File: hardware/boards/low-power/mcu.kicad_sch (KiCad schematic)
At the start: 29 parts, among them J6 Conn_01x03_Pin, SW1 SW_Push, U4 RP2040, U5 W25Q128JVPIQ, Y2 12 MHz

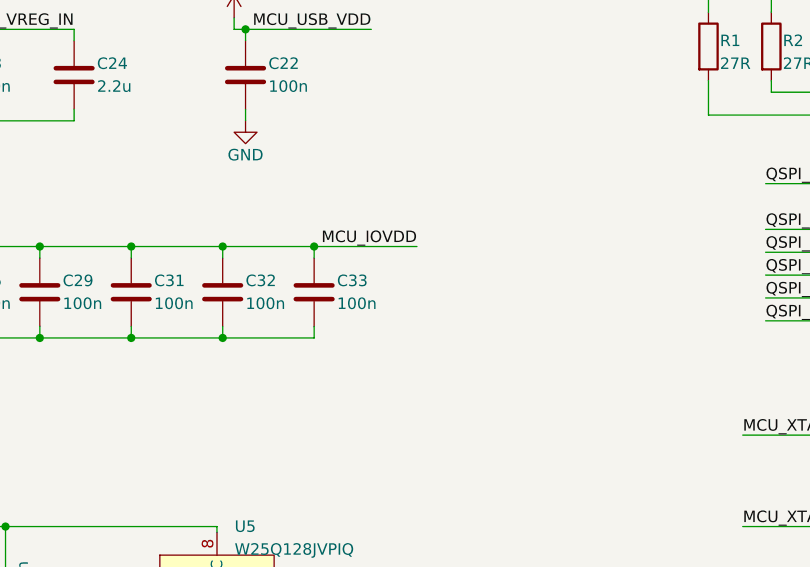
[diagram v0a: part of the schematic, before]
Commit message: Add footprints and models for LP board
Also completed rough layout for LP board to estimate board space usage.
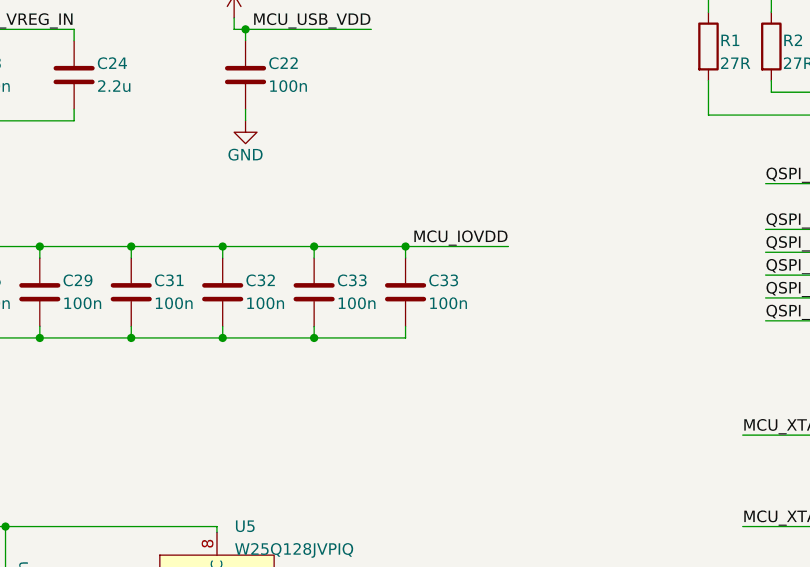
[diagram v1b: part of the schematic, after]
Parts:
- added C33: 100n, Capacitor_SMD:C_0201_0603Metric, symbol Device:C
- C1: footprint Capacitor_SMD:C_0201_0603Metric -> Capacitor_SMD:C_0402_1005Metric
- J6: footprint Connector_PinSocket_1.27mm:PinSocket_1x05_P1.27mm_Vertical -> Connector_PinHeader_1.27mm:PinHeader_1x03_P1.27mm_Vertical
- SW1: footprint (none) -> capstone:R-668048
- U5: footprint capstone:SON127P610X510X80-8N430X340 -> Package_SON:WSON-8-1EP_6x5mm_P1.27mm_EP3.4x4.3mm
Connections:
- net +3V3: now also C33.1
- net GND: now also C33.2
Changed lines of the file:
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@@
   (junction (at 33.655 93.345) (diameter 0) (color 0 0 0 0)
   )
+  (junction (at 74.295 93.345) (diameter 0) (color 0 0 0 0)
+  )
   (junction (at 132.08 134.62) (diameter 0) (color 0 0 0 0)
   )
@@
   (junction (at 59.055 164.465) (diameter 0) (color 0 0 0 0)
   )
+  (junction (at 84.455 83.185) (diameter 0) (color 0 0 0 0)
+  )
   (junction (at 33.655 43.815) (diameter 0) (color 0 0 0 0)
   )
@@
     (stroke (width 0) (type default))
   )
+  (wire (pts (xy 84.455 83.185) (xy 84.455 84.455))
+    (stroke (width 0) (type default))
+  )
   (wire (pts (xy 43.815 33.655) (xy 33.655 33.655))
     (stroke (width 0) (type default))
@@
     (stroke (width 0) (type default))
   )
+  (wire (pts (xy 84.455 92.075) (xy 84.455 93.345))
+    (stroke (width 0) (type default))
+  )
   (wire (pts (xy 66.675 67.945) (xy 66.675 69.215))
     (stroke (width 0) (type default))
@@
     (stroke (width 0) (type default))
   )
-  (wire (pts (xy 74.295 83.185) (xy 85.725 83.185))
+  (wire (pts (xy 74.295 83.185) (xy 84.455 83.185))
     (stroke (width 0) (type default))
   )
@@
     (stroke (width 0) (type default))
   )
+  (wire (pts (xy 84.455 83.185) (xy 95.885 83.185))
+    (stroke (width 0) (type default))
+  )
   (wire (pts (xy 121.92 104.14) (xy 134.62 104.14))
     (stroke (width 0) (type default))
@@
   )
   (wire (pts (xy 264.795 111.125) (xy 264.795 109.855))
+    (stroke (width 0) (type default))
+  )
+  (wire (pts (xy 84.455 93.345) (xy 74.295 93.345))
     (stroke (width 0) (type default))
   )
@@
     (effects (font (size 1.27 1.27)) (justify left bottom))
   )
-  (label "MCU_IOVDD" (at 85.725 83.185 180) (fields_autoplaced)
+  (label "MCU_IOVDD" (at 95.885 83.185 180) (fields_autoplaced)
     (effects (font (size 1.27 1.27)) (justify right bottom))
   )
@@
       (effects (font (size 1.27 1.27)))
     )
-    (property "Footprint" "" (at 45.72 159.385 0)
+    (property "Footprint" "capstone:R-668048" (at 45.72 159.385 0)
       (effects (font (size 1.27 1.27)) hide)
     )
@@
       (effects (font (size 1.27 1.27)) (justify left))
     )
-    (property "Footprint" "capstone:SON127P610X510X80-8N430X340" (at 67.31 127.635 0)
+    (property "Footprint" "Package_SON:WSON-8-1EP_6x5mm_P1.27mm_EP3.4x4.3mm" (at 67.31 127.635 0)
       (effects (font (size 1.27 1.27)) hide)
     )
@@
       (effects (font (size 1.27 1.27)))
     )
-    (property "Footprint" "Connector_PinSocket_1.27mm:PinSocket_1x05_P1.27mm_Vertical" (at 125.095 127 0)
+    (property "Footprint" "Connector_PinHeader_1.27mm:PinHeader_1x03_P1.27mm_Vertical" (at 125.095 127 0)
       (effects (font (size 1.27 1.27)) hide)
     )
@@
       (effects (font (size 1.27 1.27)) (justify left))
     )
-    (property "Footprint" "Capacitor_SMD:C_0201_0603Metric" (at 33.9852 128.27 0)
+    (property "Footprint" "Capacitor_SMD:C_0402_1005Metric" (at 33.9852 128.27 0)
       (effects (font (size 1.27 1.27)) hide)
     )
@@
         )
       )
+    )
+  )
+  (symbol (lib_id "Device:C") (at 84.455 88.265 0) (unit 1)
+    (in_bom yes) (on_board yes) (dnp no)
+    (property "Reference" "C33" (at 86.995 86.995 0)
+      (effects (font (size 1.27 1.27)) (justify left))
+    )
+    (property "Value" "100n" (at 86.995 89.535 0)
+      (effects (font (size 1.27 1.27)) (justify left))
+    )
+    (property "Footprint" "Capacitor_SMD:C_0201_0603Metric" (at 85.4202 92.075 0)
+      (effects (font (size 1.27 1.27)) hide)
+    )
+    (property "Datasheet" "~" (at 84.455 88.265 0)
+      (effects (font (size 1.27 1.27)) hide)
+    )
+    (pin "1")
+    (pin "2")
+    (instances
+      (project "nova-hw"
+        (path "/4886eafa-3297-4665-810c-164d024ecad9"
+          (reference "C33") (unit 1)
+        )
+      )
+      (project "low-power"
+        (path "/71f6a5b4-1ac6-435b-9486-30b16ab86e62"
+          (reference "C38") (unit 1)
+        )
+        (path "/71f6a5b4-1ac6-435b-9486-30b16ab86e62/fdfb7781-e4b6-4600-81c7-3705f0c2b582"
+          (reference "C68") (unit 1)
+        )
+      )

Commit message: Add initial changes after schematic review
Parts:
- added R501: 10k, Resistor_SMD:R_0201_0603Metric, symbol Device:R
- added R505: 100R, Resistor_SMD:R_0402_1005Metric, symbol Device:R
- R10, R13, R20, R3: footprint Resistor_SMD:R_0201_0603Metric -> Resistor_SMD:R_0402_1005Metric
- renumbered C38 to C511, J6 to J501, SW1 to SW501, U5 to U501
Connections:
- net +3V3: now also R501.1
- net MCU_XTAL_B: now also R505.1; no longer C26.1, Y2.3
- net VIDEO_RX: now also U4.36 (GPIO24); no longer U4.37 (GPIO25)
- net VIDEO_TX: now also U4.37 (GPIO25); no longer U4.36 (GPIO24)
- net +1V8 renamed RUN
- net RUN: now also R501.2
- new net: C26.1, R505.2, Y2.3
